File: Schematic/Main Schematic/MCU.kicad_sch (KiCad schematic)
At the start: 12 parts, among them J5 Conn_01x02_Pin, U3 CH340C, U6 M24C16-RMN6TP

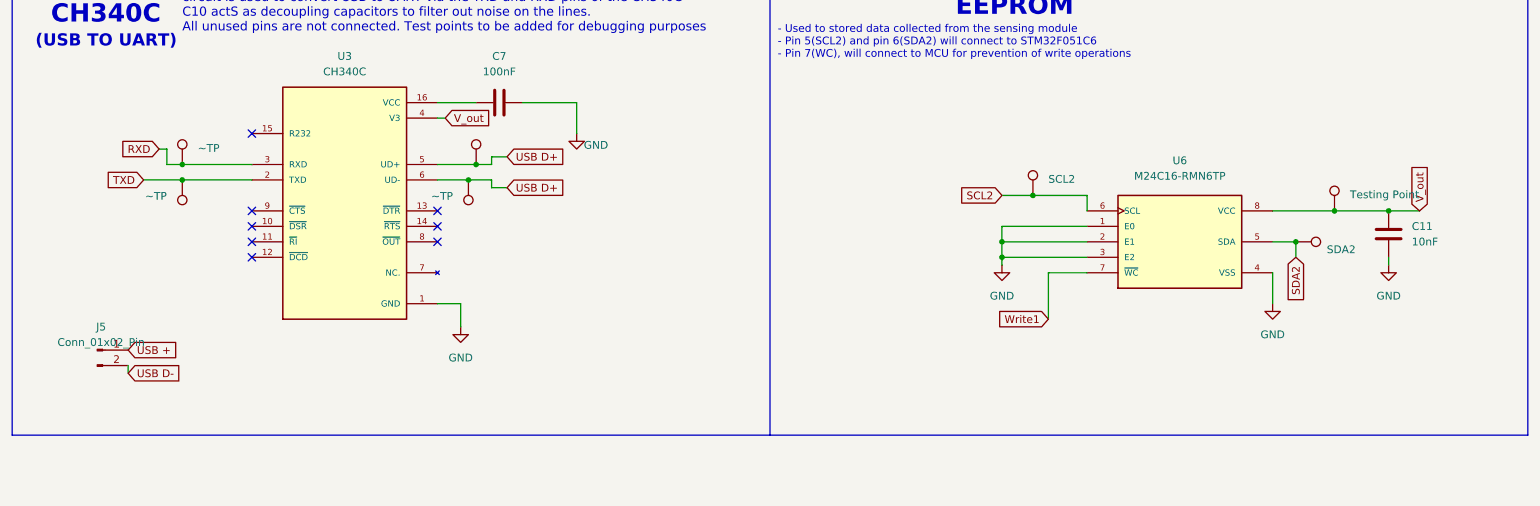
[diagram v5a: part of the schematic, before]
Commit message: I have added net lables and hierachy labels on the main schmeatic
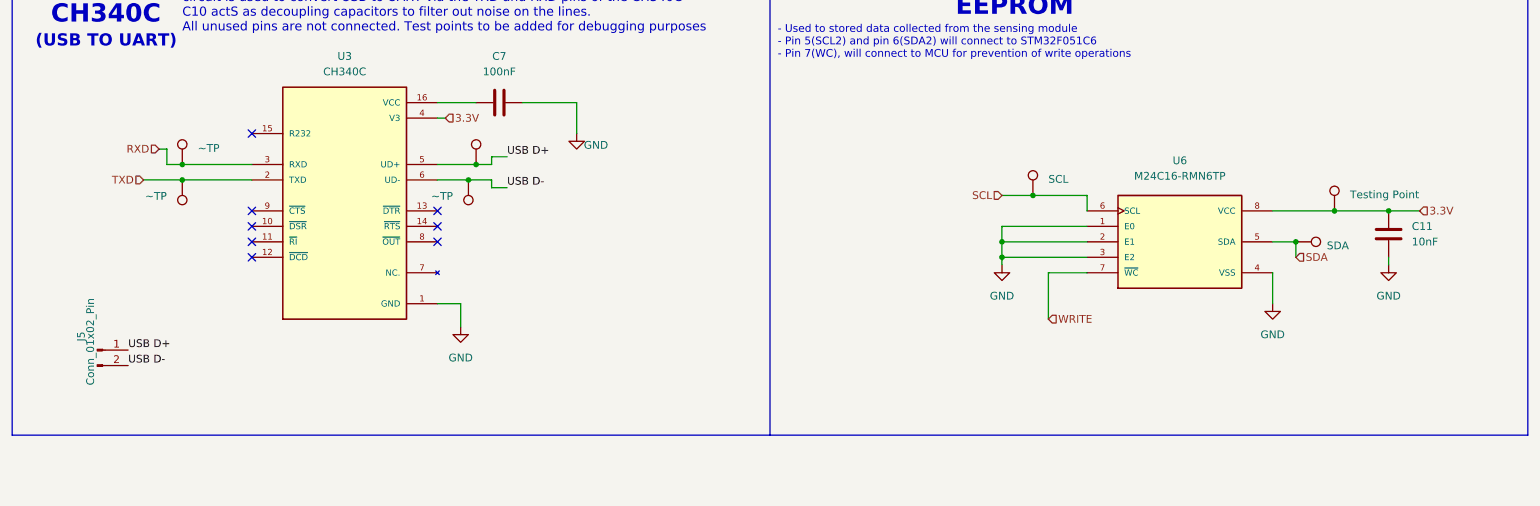
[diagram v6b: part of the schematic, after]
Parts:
- TP: value SDA2 -> SDA
- TP2: value SCL2 -> SCL
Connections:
- net USB + is gone; now on net USB D+: J5.1 (Pin_1)
- net USB D+: no longer TP6.1, U3.6 (UD-)
- net USB D-: now also TP6.1, U3.6 (UD-)
- net SCL2 renamed SCL
- net SDA2 renamed SDA
- net V_out renamed 3.3V
- net Write1 renamed WRITE
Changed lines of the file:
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@@
-    (stroke (width 0) (type default))
-  )
-  (wire (pts (xy 43.18 86.36) (xy 43.18 85.09))
     (stroke (width 0) (type default))
   )
@@
     (effects (font (size 3 3) (thickness 0.6) bold) (justify left bottom))
   )
-  (global_label "USB D+" (shape input) (at 105.41 55.88 0) (fields_autoplaced)
+  (label "USB D+" (at 43.18 82.55 0) (fields_autoplaced)
+    (effects (font (size 1.27 1.27)) (justify left bottom))
+  )
+  (label "USB D-" (at 43.18 85.09 0) (fields_autoplaced)
+    (effects (font (size 1.27 1.27)) (justify left bottom))
+  )
+  (label "USB D+" (at 105.41 50.8 0) (fields_autoplaced)
+    (effects (font (size 1.27 1.27)) (justify left bottom))
+  )
+  (label "USB D-" (at 105.41 55.88 0) (fields_autoplaced)
+    (effects (font (size 1.27 1.27)) (justify left bottom))
+  )
+  (hierarchical_label "SCL" (shape input) (at 186.69 57.15 180) (fields_autoplaced)
+    (effects (font (size 1.27 1.27)) (justify right))
+  )
+  (hierarchical_label "SDA" (shape input) (at 234.95 67.31 0) (fields_autoplaced)
     (effects (font (size 1.27 1.27)) (justify left))
-    (property "Intersheetrefs" "${INTERSHEET_REFS}" (at 115.7302 55.88 0)
-      (effects (font (size 1.27 1.27)) (justify left) hide)
-    )
-  )
-  (global_label "V_out" (shape input) (at 95.25 44.45 0) (fields_autoplaced)
+  )
+  (hierarchical_label "WRITE" (shape input) (at 194.31 77.47 0) (fields_autoplaced)
     (effects (font (size 1.27 1.27)) (justify left))
-    (property "Intersheetrefs" "${INTERSHEET_REFS}" (at 103.2357 44.45 0)
-      (effects (font (size 1.27 1.27)) (justify left) hide)
-    )
-  )
-  (global_label "USB D-" (shape input) (at 43.18 86.36 0) (fields_autoplaced)
+  )
+  (hierarchical_label "TXD" (shape input) (at 45.72 54.61 180) (fields_autoplaced)
+    (effects (font (size 1.27 1.27)) (justify right))
+  )
+  (hierarchical_label "3.3V" (shape input) (at 95.25 44.45 0) (fields_autoplaced)
     (effects (font (size 1.27 1.27)) (justify left))
-    (property "Intersheetrefs" "${INTERSHEET_REFS}" (at 53.5002 86.36 0)
-      (effects (font (size 1.27 1.27)) (justify left) hide)
-    )
-  )
-  (global_label "SDA2" (shape input) (at 234.95 67.31 270) (fields_autoplaced)
+  )
+  (hierarchical_label "RXD" (shape input) (at 48.26 49.53 180) (fields_autoplaced)
     (effects (font (size 1.27 1.27)) (justify right))
-    (property "Intersheetrefs" "${INTERSHEET_REFS}" (at 235.0294 74.5007 90)
-      (effects (font (size 1.27 1.27)) (justify right) hide)
-    )
-  )
-  (global_label "SCL2" (shape input) (at 186.69 57.15 180) (fields_autoplaced)
-    (effects (font (size 1.27 1.27)) (justify right))
-    (property "Intersheetrefs" "${INTERSHEET_REFS}" (at 179.0671 57.15 0)
-      (effects (font (size 1.27 1.27)) (justify right) hide)
-    )
-  )
-  (global_label "Write1" (shape input) (at 194.31 77.47 180) (fields_autoplaced)
-    (effects (font (size 1.27 1.27)) (justify right))
-    (property "Intersheetrefs" "${INTERSHEET_REFS}" (at 186.0307 77.3906 0)
-      (effects (font (size 1.27 1.27)) (justify right) hide)
-    )
-  )
-  (global_label "USB D+" (shape input) (at 105.41 50.8 0) (fields_autoplaced)
+  )
+  (hierarchical_label "3.3V" (shape input) (at 255.27 59.69 0) (fields_autoplaced)
     (effects (font (size 1.27 1.27)) (justify left))
-    (property "Intersheetrefs" "${INTERSHEET_REFS}" (at 115.7302 50.8 0)
-      (effects (font (size 1.27 1.27)) (justify left) hide)
-    )
-  )
-  (global_label "V_out" (shape input) (at 255.27 59.69 90) (fields_autoplaced)
-    (effects (font (size 1.27 1.27)) (justify left))
-    (property "Intersheetrefs" "${INTERSHEET_REFS}" (at 255.1906 52.1969 90)
-      (effects (font (size 1.27 1.27)) (justify left) hide)
-    )
-  )
-  (global_label "RXD" (shape input) (at 48.26 49.53 180) (fields_autoplaced)
-    (effects (font (size 1.27 1.27)) (justify right))
-    (property "Intersheetrefs" "${INTERSHEET_REFS}" (at 42.0974 49.6094 0)
-      (effects (font (size 1.27 1.27)) (justify right) hide)
-    )
-  )
-  (global_label "TXD" (shape input) (at 45.72 54.61 180) (fields_autoplaced)
-    (effects (font (size 1.27 1.27)) (justify right))
-    (property "Intersheetrefs" "${INTERSHEET_REFS}" (at 39.8598 54.6894 0)
-      (effects (font (size 1.27 1.27)) (justify right) hide)
-    )
-  )
-  (global_label "USB +" (shape input) (at 43.18 82.55 0) (fields_autoplaced)
-    (effects (font (size 1.27 1.27)) (justify left))
-    (property "Intersheetrefs" "${INTERSHEET_REFS}" (at 52.2302 82.55 0)
-      (effects (font (size 1.27 1.27)) (justify left) hide)
-    )
   )
   (symbol (lib_id "power:GND") (at 231.14 74.93 0) (unit 1)
@@
       (effects (font (size 1.27 1.27)) (justify left) hide)
     )
-    (property "Value" "SDA2" (at 240.03 66.0399 90)
+    (property "Value" "SDA" (at 240.03 65.405 90)
       (effects (font (size 1.27 1.27)) (justify left))
     )
@@
   )
   (symbol (lib_id "Connector:Conn_01x02_Pin") (at 38.1 82.55 0) (unit 1)
-    (in_bom yes) (on_board yes) (dnp no) (fields_autoplaced)
-    (property "Reference" "J5" (at 38.735 78.74 0)
-      (effects (font (size 1.27 1.27)))
-    )
-    (property "Value" "Conn_01x02_Pin" (at 38.735 81.28 0)
+    (in_bom yes) (on_board yes) (dnp no)
+    (property "Reference" "J5" (at 35.4584 80.3148 90)
+      (effects (font (size 1.27 1.27)))
+    )
+    (property "Value" "Conn_01x02_Pin" (at 36.9824 81.1784 90)
       (effects (font (size 1.27 1.27)))
     )
@@
       (effects (font (size 1.27 1.27)) (justify left) hide)
     )
-    (property "Value" "SCL2" (at 194.31 54.483 0)
+    (property "Value" "SCL" (at 194.31 54.483 0)
       (effects (font (size 1.27 1.27)) (justify left))
     )

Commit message: Update
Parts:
- removed TP: SDA, TestPoint:TestPoint_Pad_1.0x1.0mm, symbol Connector:TestPoint
- removed TP1: Testing Point, TestPoint:TestPoint_Pad_1.0x1.0mm, symbol Connector:TestPoint
- removed TP2: SCL, TestPoint:TestPoint_Pad_1.0x1.0mm, symbol Connector:TestPoint
- removed TP3: ~TP, TestPoint:TestPoint_Pad_1.0x1.0mm, symbol Connector:TestPoint
- removed U3: CH340C, CH340:SOIC127P600X180-16N, symbol CH340C:CH340C
- added TP10, TP11, TP12, TP13, TP9: TestPoint, symbol Connector:TestPoint
- added U3: CH340C, Package_SO:SOIC-16_3.9x9.9mm_P1.27mm, symbol Interface_USB:CH340C
- TP5, TP6: value ~TP -> TestPoint; footprint TestPoint:TestPoint_Pad_1.0x1.0mm -> (none)
- TP7: value ~ -> TestPoint; footprint TestPoint:TestPoint_Pad_1.0x1.0mm -> (none)
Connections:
- net 3.3V: now also TP9.1, U3.4 (V3)
- net GND: now also C7.1, U3.1 (GND); no longer C7.2
- net RXD: now also TP13.1, U3.3 (RXD)
- net SCL: now also TP10.1
- net SDA: now also TP11.1
- net TXD: now also U3.2 (TXD)
- net USB D+: now also U3.6 (UD-)
- net USB D-: now also U3.5 (UD+)
- net WRITE: now also TP12.1
- new net: C7.2, U3.16 (VCC)
- no-connect marks 8 -> 7
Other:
- moved on the sheet: C7

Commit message: update
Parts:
- removed C11: 10nF, CAP_10NF:CAPC1005X55N, symbol Device:C
- removed C7: 100nF, 100NF_C:CAPC1005X55N, symbol Device:C
- removed J5: Conn_01x02_Pin, symbol Connector:Conn_01x02_Pin
- removed U6: M24C16-RMN6TP, M24:SOIC127P600X175-8N, symbol M24C16-RMN6TP:M24C16-RMN6TP
- added C7: 100nF, 100NF_C:CAPC1005X55N, symbol Device:C
- added C7: 10nF, CAP_10NF:CAPC1005X55N, symbol Device:C
- added J1: Conn_01x02_Pin, symbol Connector:Conn_01x02_Pin
- added U4: M24C16-RMN6TP, M24:SOIC127P600X175-8N, symbol M24C16-RMN6TP:M24C16-RMN6TP
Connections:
- net 3.3V: now also TP13.1, C7.1, U4.8 (VCC); no longer TP9.1
- net GND: now also C7.1, C7.2, U4.1 (E0), U4.2 (E1), U4.3 (E2), U4.4 (VSS)
- net RXD: now also TP7.1; no longer TP13.1
- net SCL: now also U4.6 (SCL)
- net SDA: now also TP12.1, U4.5 (SDA); no longer TP11.1
- net TXD: now also TP9.1; no longer TP5.1
- net USB D+: now also TP5.1, J1.1 (Pin_1); no longer TP7.1
- net USB D-: now also J1.2 (Pin_2)
- net WRITE: now also TP11.1, U4.7 (~{WC}); no longer TP12.1
- net at U3.16 (VCC): now also C7.2
